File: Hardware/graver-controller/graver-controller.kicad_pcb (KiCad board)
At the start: 4 copper layers, 85 x 60 mm, 117 parts, among them J101 Power in 2p, J201 Handpiece pads 1x4, J301 USB-C, J302 SWD, J401 LCD pads 1x7, J402 Pedal pads 1x4, J403 Encoder pads 1x4, Q101 DMP6023LE, Q201 IRLR3410, Q202 SI2309CDS, Q203 BSS123, SW301 BOOT0, SW302 RESET, U101 LM5164DDAR, U102 AP2112K-3.3, U201 UCC27517DBVR, U202 TLV9062IDR, U301 STM32F411CEU6, U302 USBLC6-2SC6, U401 PESD5V0S2BT, Y301 25MHz 10pF

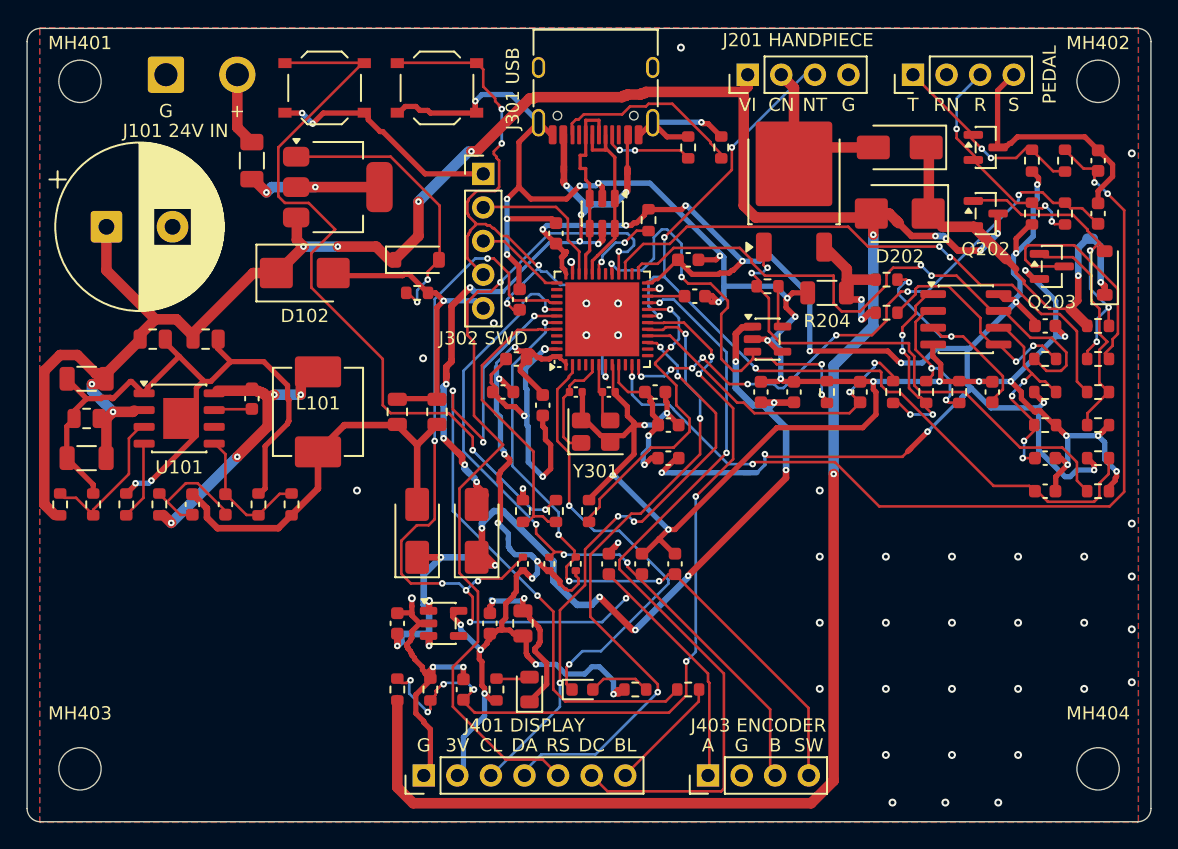
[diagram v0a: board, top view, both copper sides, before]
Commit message: pcb: ADR 0003 width floors restored and met; DRC 0/0/0 with 0 warnings
The 52 power necks were the router bending +3V3/VBUS/VDDA around signals
it had laid first, and most of what blocked widening them was the stale
GND pour (widen.py now refills before judging). tools/pcb5/floors.py rips
the five signal nets in the way (LCD_SCK, ENC_SW, LCD_BL, LCD_RST, the
op-amp feedback, PEDAL_TIP east of the MCU), re-draws the R404 stub and
the VDDA run, widens the rest to class width, and adds the 'fine-pitch'
rule areas; krt-reroute --keep re-lays the signals around the wider
copper.

.kicad_dru is back at ADR 0003's floors: 0.5 mm HighCurrent, 0.3 mm 5V and
3V3 classes, with 0.2 mm only inside the fine-pitch areas (ADR 0003 D5's own
rule for the QFN48 and USB-C) and signal widths on the CLAMP gate-bias
branch. check.py checks the same. +3V3 and VDDA are at the full 0.4 mm
class width on every segment outside those areas; VBUS min 0.4, +5V 0.5.
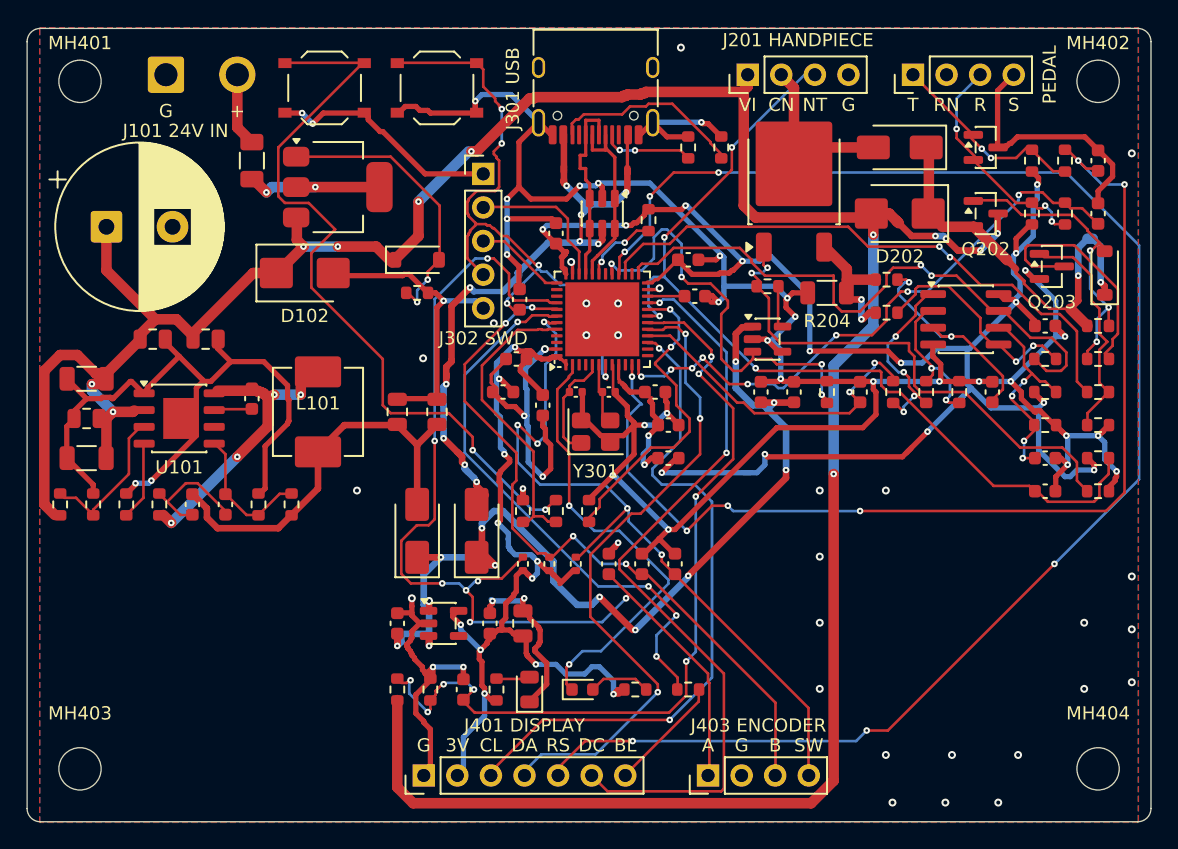
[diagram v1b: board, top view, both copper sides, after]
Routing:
- net LCD_RST: track 63.0 -> 117.5 mm, vias 2 -> 6
- net LCD_BL: track 53.4 -> 42.7 mm
- net PEDAL_TIP: track 71.3 -> 80.2 mm, vias 4 -> 6
- net LCD_SCK: track 43.8 -> 50.4 mm, vias 5 -> 2
- net ENC_SW: track 51.1 -> 56.5 mm, vias 4 -> 5
- net +3V3: track 223.6 -> 222.1 mm
- net /MCU/VDDA: track 11.4 -> 11.9 mm
- net GND: vias 77 -> 67

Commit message: graver pcb: F101 -> 1206L035/30WR PTC; the 0437001.WR is a fast fuse and blows on hot-plug inrush
Board 1 blew F101 on the first 24 V connect. The 437 series is fast-acting
(1 A, I2t 0.100 A2s), not Slo-Blo as the parts doc said; hot-plugging 24 V
into C101 470 uF is roughly 0.27-0.45 A2s. A 1206 PTC (0.35 A hold, 30 V,
Imax 100 A) ignores the inrush pulse and resets after a fault. Same footprint,
so the 12 built boards take it as a one-part swap. fab/ is left as built.
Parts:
- F101: value 1A slow -> PTC 0.35A 30V
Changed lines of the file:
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@@
 			)
 		)
-		(property "Value" "1A slow"
+		(property "Value" "PTC 0.35A 30V"
 			(at 0 1.83 270)
 			(layer "F.Fab")
@@
 			)
 		)
-		(property "Description" ""
+		(property "Description" "Resettable PTC, 0.35 A hold / 0.75 A trip, 30 V, Imax 100 A; survives hot-plug inrush into C101"
 			(at 0 0 270)
 			(layer "F.Fab")
@@
 			)
 		)
-		(property "LCSC" "C99537"
+		(property "LCSC" "C2153989"
 			(at 0 0 270)
 			(layer "F.Fab")
@@
 			)
 		)
-		(property "MPN" "0437001.WR"
+		(property "MPN" "1206L035/30WR"
 			(at 0 0 270)
 			(layer "F.Fab")
